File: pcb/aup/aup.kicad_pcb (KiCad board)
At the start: 6 copper layers, 100 x 100 mm, 116 parts, among them IC1 MT41K128M16JT-125_K, IC2 88E1512-A0-NNP2C000, J1 DF40C-100DS-0.4V_51, J2 DF40C-100DS-0.4V_51, J3 DF40C-100DS-0.4V_51, J4 DF40C-100DS-0.4V_51, Q1 AO3401A, Q2 AO3401A, U1 XC7A50T-FGG484, U10 TPS563257DRLR, U11 FT2232HQ, U12 93LC56BT-I/OT, U13 MX25L3233FM2, U2 USBLC6-2SC6, U3 TPS563257DRLR, U4 TPS563257DRLR, U5 TPS563257DRLR, U6 TPS563257DRLR, U7 TPS563257DRLR, U8 TPS563257DRLR, U9 TPS563257DRLR, Y1 12MHz/20pf

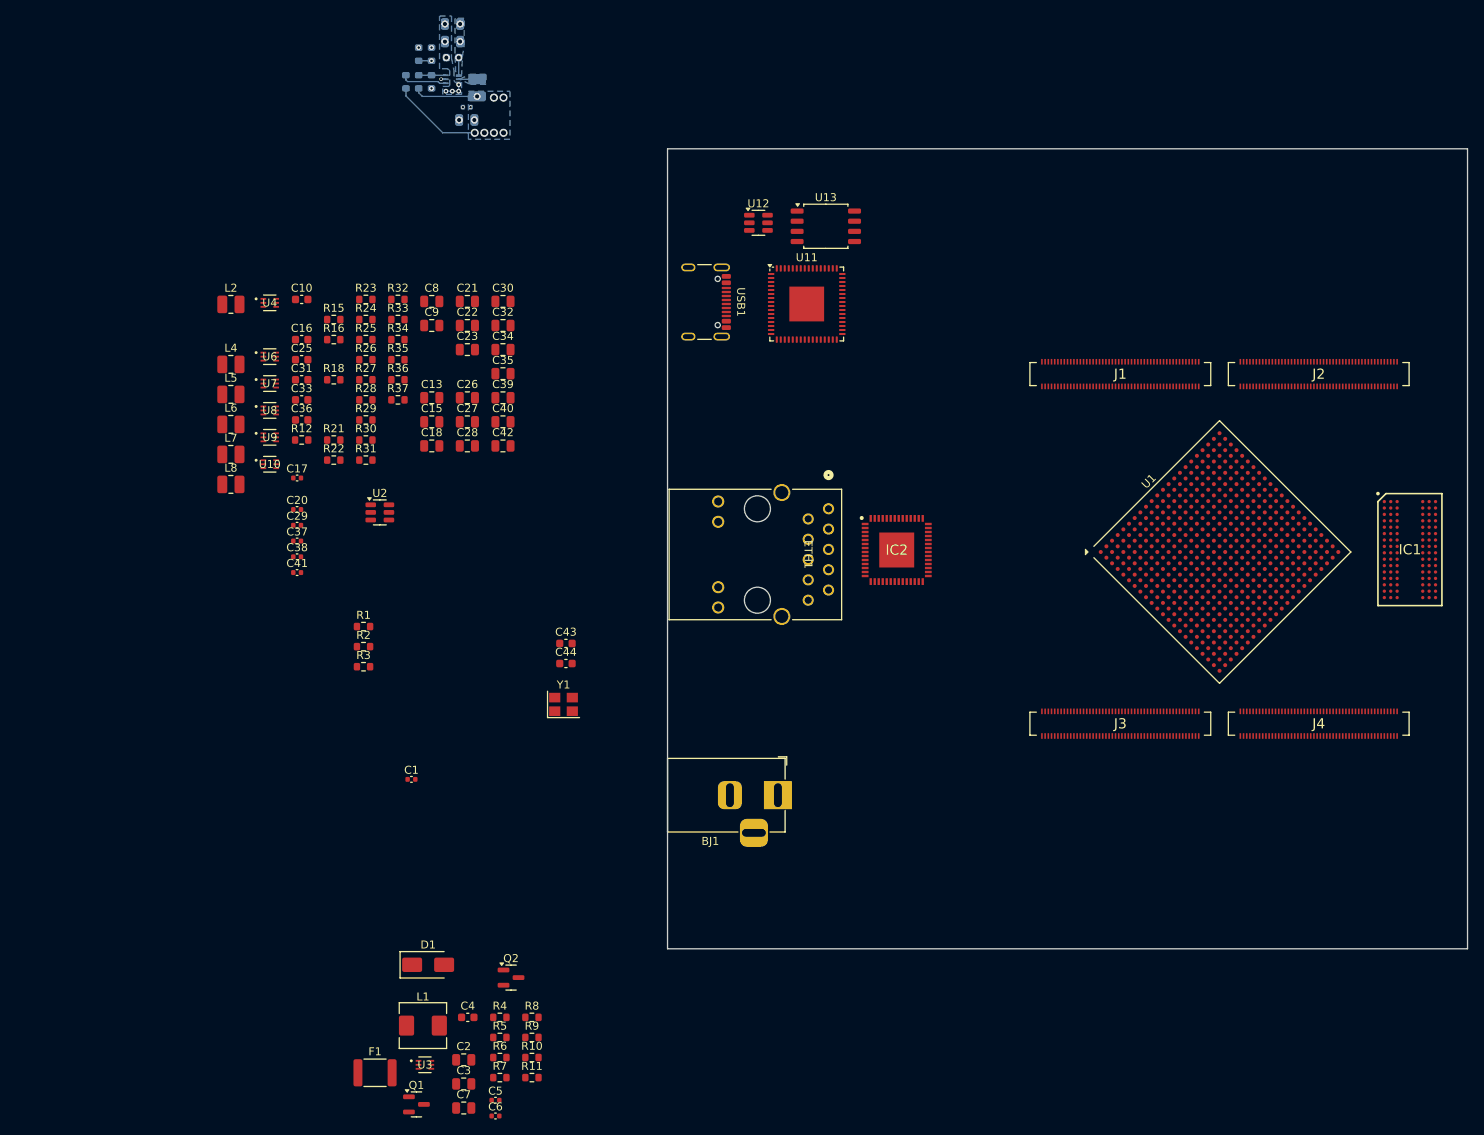
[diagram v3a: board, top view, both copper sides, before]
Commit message: Redo high level layout for, hopefully, better power routing
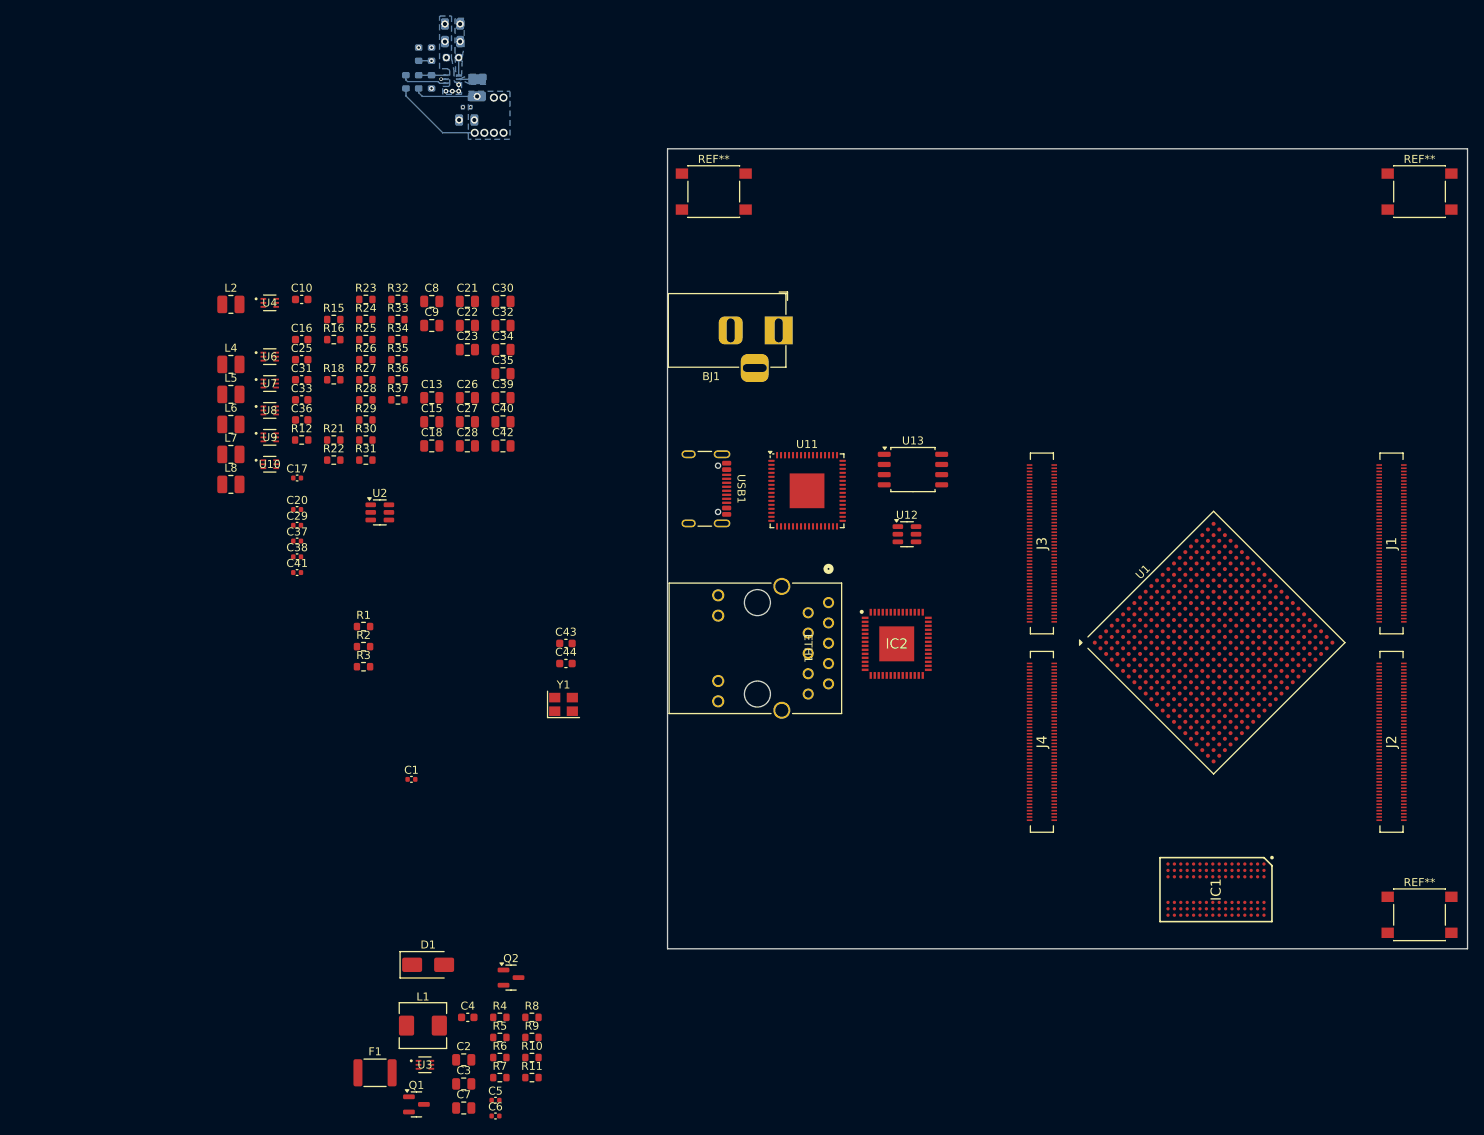
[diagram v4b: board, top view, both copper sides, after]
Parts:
- added REF**: SW_SPST_PTS645, Button_Switch_SMD:SW_SPST_PTS645, F.Cu at (194.0, 126.8)
- added REF**: SW_SPST_PTS645, Button_Switch_SMD:SW_SPST_PTS645, F.Cu at (194.0, 36.4)
- added REF**: SW_SPST_PTS645, Button_Switch_SMD:SW_SPST_PTS645, F.Cu at (105.8, 36.4)
- moved BJ1 58.1 mm to (113.9, 53.7)
- moved IC1 48.9 mm to (168.6, 123.6), turned to -90 degrees
- moved J2 46.9 mm to (190.5, 105.1), turned to -90 degrees
- moved U12 43.1 mm to (129.9, 79.2)
- moved J1 40.0 mm to (190.5, 80.3), turned to -90 degrees
- moved J4 34.7 mm to (146.8, 105.1), turned to -90 degrees
- moved U13 32.3 mm to (130.7, 71.1)
- moved J3 24.6 mm to (146.8, 80.3), turned to -90 degrees
- moved U11 23.4 mm to (117.4, 73.8)
- moved USB1 23.4 mm to (103.7, 73.5)
- moved ETH1 11.7 mm to (120.1, 87.7)
- moved IC2 11.7 mm to (128.7, 92.9)
- moved U1 11.4 mm to (168.3, 92.7)

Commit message: First pass on upper voltage rails
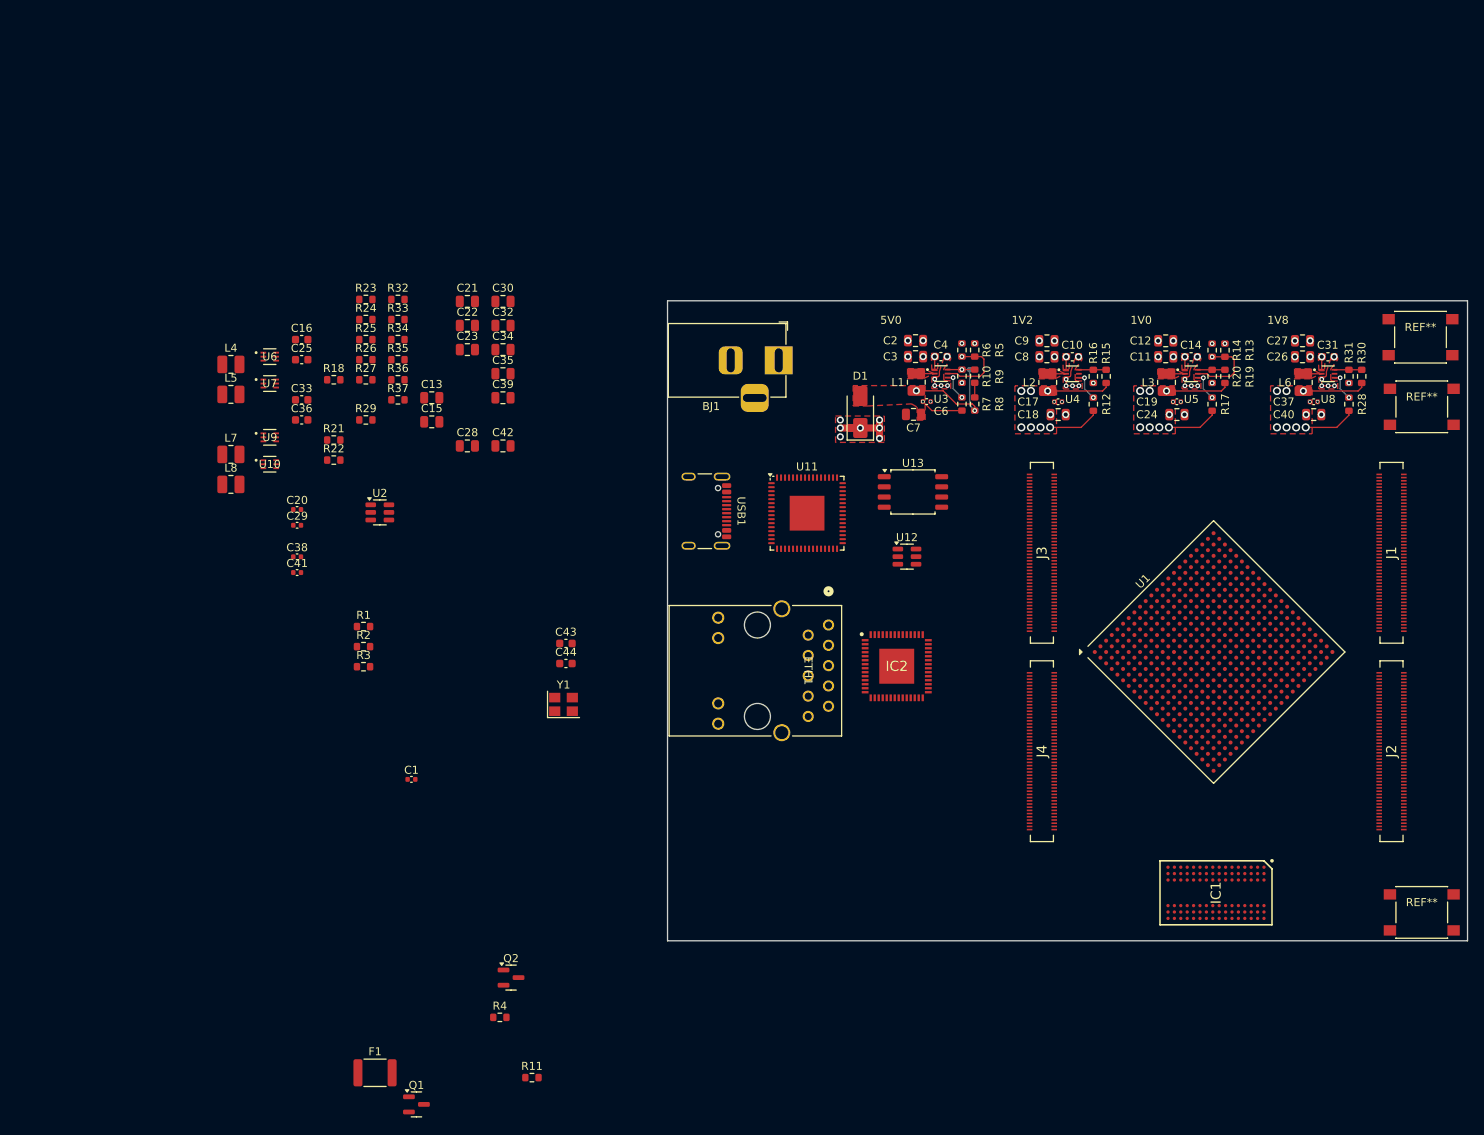
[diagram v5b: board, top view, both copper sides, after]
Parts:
- removed the REF** at (194.0, 126.8)
- removed the REF** at (194.0, 36.4)
- removed the REF** at (105.8, 36.4)
- added REF**: SW_SPST_PTS645, Button_Switch_SMD:SW_SPST_PTS645, F.Cu at (194.1, 54.5)
- added REF**: SW_SPST_PTS645, Button_Switch_SMD:SW_SPST_PTS645, F.Cu at (194.3, 126.5)
- added REF**: SW_SPST_PTS645, Button_Switch_SMD:SW_SPST_PTS645, F.Cu at (194.3, 63.2)
- C11, C12, C14, C19, C24, L3, R13, R14, R17, R19, R20, U5: moved to F.Cu
- C5: moved to B.Cu
- L1: footprint Inductor_SMD:L_Sunlord_MWSA0518S -> Inductor_SMD:L_1008_2520Metric
- moved L6 134.2 mm to (179.5, 60.2), turned to -90 degrees
- moved U8 132.4 mm to (182.6, 59.1)
- moved C31 128.3 mm to (182.6, 57.0)
- moved C37 128.3 mm to (180.8, 62.6)
- moved R30 124.7 mm to (186.8, 59.4), turned to 90 degrees
- moved R31 123.3 mm to (185.2, 59.4), turned to -90 degrees
- moved R28 122.9 mm to (185.2, 62.9), turned to -90 degrees
- moved C5 108.6 mm to (137.3, 58.6), turned to 180 degrees
- moved R17 108.5 mm to (168.1, 62.9)
- moved U3 107.8 mm to (134.2, 59.1)
- moved R13 107.4 mm to (169.7, 56.2)
- moved R19 107.3 mm to (169.7, 59.4)
- moved C3 107.0 mm to (131.0, 57.0), turned to 180 degrees
- moved C2 106.2 mm to (131.0, 55.0), turned to 180 degrees
- moved R6 105.6 mm to (136.8, 56.2), turned to 90 degrees
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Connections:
- net /ext_power/5V4_REG renamed /ext_power/REG_5V4
- net /ext_power/5V_SW renamed /ext_power/SW_5V4
- net /ext_power/5V_USB renamed /ext_power/USB_5V
- net Net-(Q1-S) renamed /ext_power/PROT_12V
- net Net-(U3-EN) renamed /ext_power/EN_4V4
- net Net-(U3-FB) renamed /ext_power/FB_5V4
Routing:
- net /ext_power/REG_5V4: track 0.00 -> 19.4 mm, vias 0 -> 3
- net +1V2: track 0.00 -> 14.6 mm, vias 0 -> 9
- net +Vccaux: track 0.00 -> 14.6 mm, vias 0 -> 9
- net +5V: track 2.20 -> 16.3 mm, vias 4 -> 17
- net /ext_power/EN_4V4: track 0.00 -> 9.45 mm, vias 0 -> 1
- net GND: track 2.60 -> 10.4 mm, vias 11 -> 41
- net /power_reg/EN_Vccint: track 2.24 -> 9.45 mm, vias 2 -> 1
- net +Vccint: track 19.5 -> 14.6 mm
- net Net-(U3-PG): track 0.00 -> 3.64 mm, vias 0 -> 2
- net /power_reg/PG_1V2: track 0.00 -> 3.64 mm, vias 0 -> 2
- net /power_reg/PG_Vccaux: track 0.00 -> 3.64 mm, vias 0 -> 2
- net Net-(U8-FB): track 0.00 -> 3.41 mm
- net Net-(U4-FB): track 0.00 -> 3.41 mm
- net /ext_power/FB_5V4: track 0.00 -> 3.41 mm, vias 0 -> 1
- net /power_reg/SW_Vccaux: track 0.00 -> 2.30 mm
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- added copper zone on F.Cu, net +1V2
- added copper zone on F.Cu, net +5V
- added copper zone on F.Cu, net +Vccaux
- added copper zone on F.Cu, net +Vccint
- added copper zone on F.Cu, net /ext_power/PROT_12V
- added copper zone on F.Cu, net /ext_power/REG_5V4
- added copper zone on F.Cu, net /ext_power/SW_5V4
- added copper zone on F.Cu, net /power_reg/SW_1V2
- added copper zone on F.Cu, net /power_reg/SW_Vccaux
- added copper zone on F.Cu, net /power_reg/SW_Vccint
- added copper zone on F.Cu, net GND
- removed copper zone on B.Cu, net +5V
- removed copper zone on B.Cu, net +Vccint
- removed copper zone on B.Cu, net /power_reg/SW_Vccint
- removed copper zone on B.Cu, net GND
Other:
- board size 100 x 100 mm -> 100 x 80 mm
- board text added: "1V0"
- board text added: "1V2"
- board text added: "1V8"
- board text added: "5V0"

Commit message: Delete rails that aren't going to be used
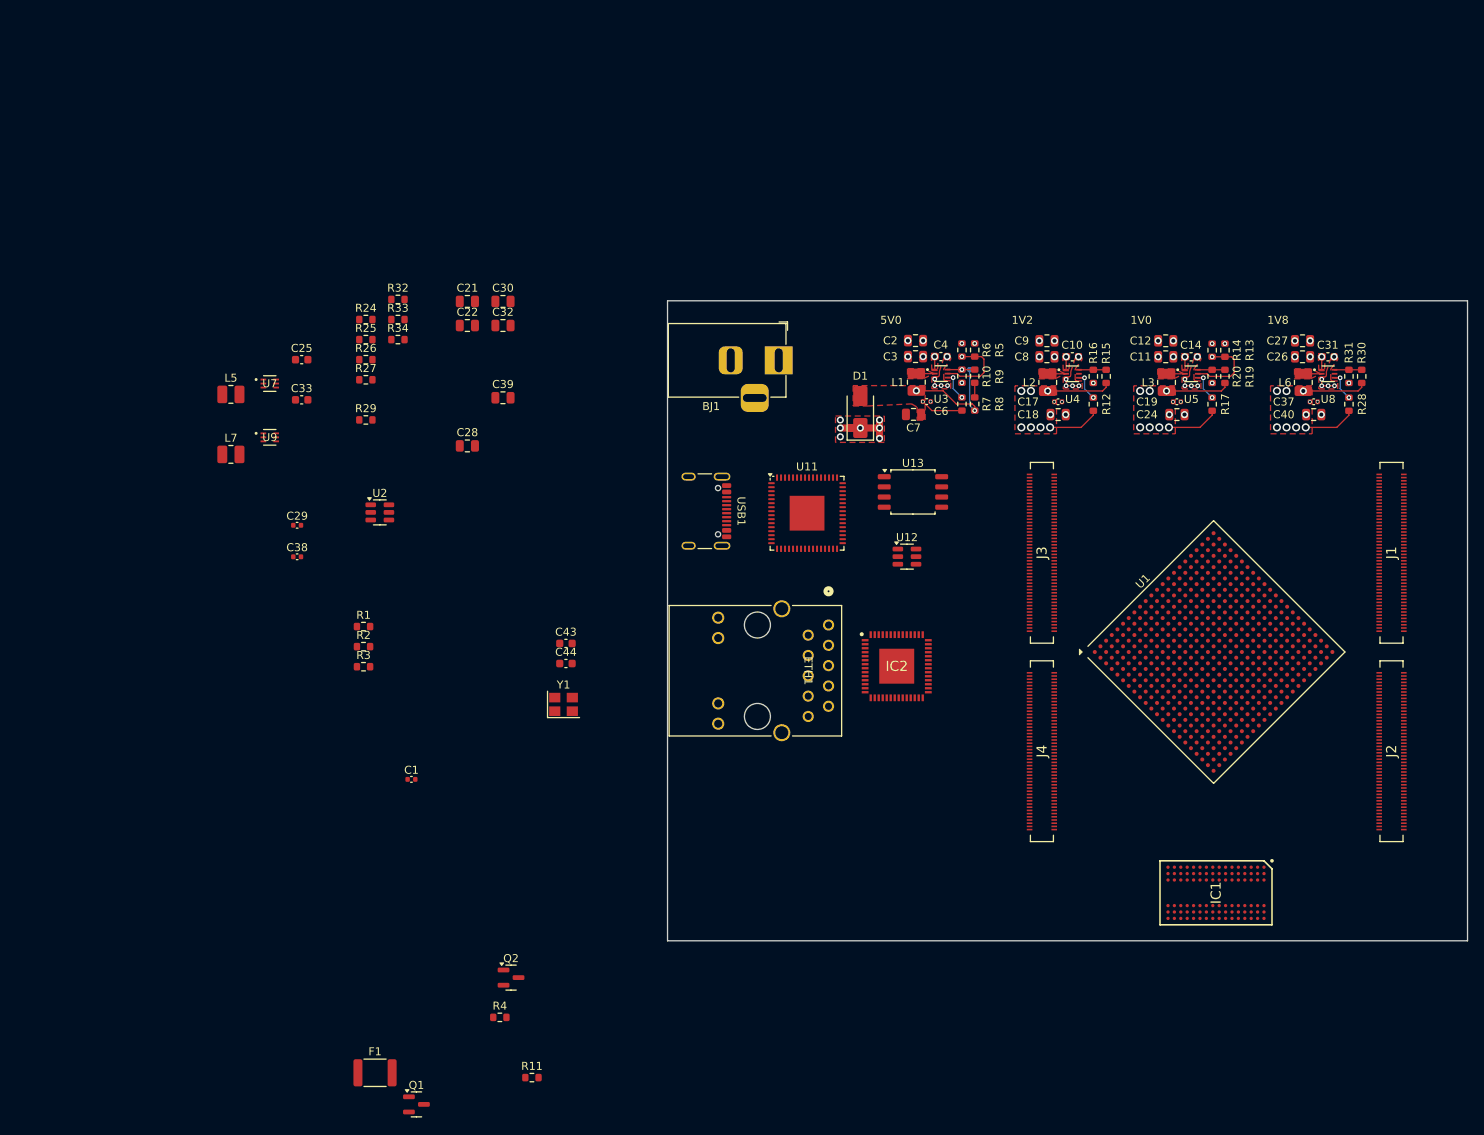
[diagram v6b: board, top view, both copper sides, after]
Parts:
- removed C13, C15, C34, C35: 10uf/50V, Capacitor_SMD:C_0805_2012Metric
- removed C16, C36: 0.1uf/50v, Capacitor_SMD:C_0603_1608Metric
- removed C20, C41: 0.1uf, Capacitor_SMD:C_0402_1005Metric
- removed C23, C42: 22uf/25V, Capacitor_SMD:C_0805_2012Metric
- removed L4: 2.2uH/2A, Inductor_SMD:L_1008_2520Metric
- removed L8: 1uH/2A, Inductor_SMD:L_1008_2520Metric
- removed R18, R35, R37: 10K, Resistor_SMD:R_0603_1608Metric
- removed R21: 43K, Resistor_SMD:R_0603_1608Metric
- removed R22: 4.99K, Resistor_SMD:R_0603_1608Metric
- removed R23: 15K, Resistor_SMD:R_0603_1608Metric
- removed R36: 20K, Resistor_SMD:R_0603_1608Metric
- removed REF** (x3): SW_SPST_PTS645, Button_Switch_SMD:SW_SPST_PTS645
- removed U10, U6: TPS563257DRLR, !Misc:SOT6_DRL_TEX
